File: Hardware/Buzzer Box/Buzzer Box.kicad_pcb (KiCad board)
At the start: 2 copper layers, 105.5 x 60.5 mm, 77 parts, among them IC1 4691, IC10 4691, IC11 4691, IC12 4691, IC2 4691, IC3 4691, IC4 4691, IC5 4691, IC6 4691, IC7 4691, IC8 4691, IC9 4691, J1 GPIO 2 + GND, J10 Conn_01x03_Socket, J11 USB_C_Receptacle_USB2.0_16P, J12 GPIO 2 + GND, J15 IO42, J16 IO41, J19 GND, J2 Conn_01x03_Socket, J20 3V3, J21 24V, J22 5V, J3 Conn_01x03_Socket, J4 Conn_01x03_Socket, J5 Conn_01x03_Socket, J6 GPIO 2 + GND, J7 Conn_01x03_Socket, J8 Conn_01x03_Socket, J9 Conn_01x03_Socket, Q1 AO3400A, Q2 AO3400A, Q3 AO3400A, Q4 AO3400A, Q5 AO3400A, Q6 AO3400A, Q7 AO3400A, Q8 AO3400A, U1 LTV-817S, U10 ESP32-S3-WROOM-1, U2 USBLC6-2SC6, U3 LTV-817S, U4 LTV-817S, U5 LTV-817S, U6 LTV-817S, U7 LTV-817S, U8 LTV-817S, U9 LTV-817S

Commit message: Updated the PCB
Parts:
- removed J10, J4, J5, J7, J8, J9: Conn_01x03_Socket, Connector_JST:JST_XH_B3B-XH-AM_1x03_P2.50mm_Vertical
- removed J15: IO42, Connector_Wire:SolderWirePad_1x01_SMD_1x2mm
- removed J16: IO41, Connector_Wire:SolderWirePad_1x01_SMD_1x2mm
- added C3: 100n, Capacitor_SMD:C_0603_1608Metric_Pad1.08x0.95mm_HandSolder, F.Cu at (119.8, 116.6)
- added C4: 100n, Capacitor_SMD:C_0603_1608Metric_Pad1.08x0.95mm_HandSolder, F.Cu at (137.8, 116.6)
- added C6: 100n, Capacitor_SMD:C_0603_1608Metric_Pad1.08x0.95mm_HandSolder, F.Cu at (101.8, 116.6)
- added C7: 100n, Capacitor_SMD:C_0603_1608Metric_Pad1.08x0.95mm_HandSolder, F.Cu at (84.0, 116.6)
- added H1: MountingHole_Pad, MountingHole:MountingHole_3.2mm_M3_ISO14580_Pad_TopBottom, F.Cu at (71.0, 72.0)
- added H2: MountingHole_Pad, MountingHole:MountingHole_3.2mm_M3_ISO14580_Pad_TopBottom, F.Cu at (201.0, 73.0)
- added H3: MountingHole_Pad, MountingHole:MountingHole_3.2mm_M3_ISO14580_Pad_TopBottom, F.Cu at (197.0, 109.0)
- added H4: MountingHole_Pad, MountingHole:MountingHole_3.2mm_M3_ISO14580_Pad_TopBottom, F.Cu at (47.0, 119.0)
- added H5: MountingHole_Pad, MountingHole:MountingHole_3.2mm_M3_ISO14580_Pad_TopBottom, F.Cu at (148.0, 74.0)
- added J13: NC3FAAH, Connector_Audio:Jack_XLR_Neutrik_NC3FAAH_Horizontal, F.Cu at (158.0, 68.9)
- added J14: NC3FAAH, Connector_Audio:Jack_XLR_Neutrik_NC3FAAH_Horizontal, F.Cu at (184.0, 68.9)
- added J17: NC3FAAH, Connector_Audio:Jack_XLR_Neutrik_NC3FAAH_Horizontal, F.Cu at (210.0, 68.9)
- added J18: NC3FAAH, Connector_Audio:Jack_XLR_Neutrik_NC3FAAH_Horizontal, F.Cu at (216.0, 107.0)
- added J23: NC3FAAH, Connector_Audio:Jack_XLR_Neutrik_NC3FAAH_Horizontal, F.Cu at (132.0, 68.9)
- added J24: NC3FAAH, Connector_Audio:Jack_XLR_Neutrik_NC3FAAH_Horizontal, F.Cu at (106.0, 68.9)
- added J25: NC3FAAH, Connector_Audio:Jack_XLR_Neutrik_NC3FAAH_Horizontal, F.Cu at (80.0, 68.9)
- added J26: NC3FAAH, Connector_Audio:Jack_XLR_Neutrik_NC3FAAH_Horizontal, F.Cu at (54.0, 68.9)
- C1: footprint Capacitor_SMD:C_0603_1608Metric_Pad1.08x0.95mm_HandSolder -> Capacitor_SMD:C_0603_1608Metric
- J19, J20, J22: moved to F.Cu
- J2: value Conn_01x03_Socket -> UART; footprint Connector_JST:JST_XH_B3B-XH-AM_1x03_P2.50mm_Vertical -> Connector_JST:JST_XH_B4B-XH-A_1x04_P2.50mm_Vertical
- J21: value 24V -> 24v; moved to F.Cu
- J3: value Conn_01x03_Socket -> JTAG; footprint Connector_JST:JST_XH_B3B-XH-AM_1x03_P2.50mm_Vertical -> Connector_JST:JST_XH_B4B-XH-A_1x04_P2.50mm_Vertical
- R10, R3, R4, R5, R6, R7, R8, R9: footprint Resistor_SMD:R_0805_2012Metric -> Resistor_SMD:R_0603_1608Metric
- moved R16 89.4 mm to (98.2, 107.0), turned to 0 degrees
- moved R20 86.5 mm to (77.0, 102.1), turned to 180 degrees
- moved R17 86.2 mm to (61.8, 102.1)
- moved R18 85.8 mm to (56.8, 102.1)
- moved U11 84.7 mm to (50.6, 97.0)
- moved U12 83.5 mm to (70.8, 97.0)
- moved R19 81.7 mm to (82.0, 102.1)
- moved R2 74.3 mm to (98.2, 105.0)
- moved J2 66.7 mm to (117.5, 103.5), turned to 90 degrees
- moved C1 65.3 mm to (107.5, 105.0), turned to 180 degrees
- moved R11 65.1 mm to (107.5, 107.0), turned to 0 degrees
- moved Q8 62.6 mm to (48.4, 79.2)
- moved S1 59.4 mm to (110.0, 101.2), turned to 180 degrees
- moved U9 58.3 mm to (57.4, 80.3), turned to 180 degrees
- moved IC11 55.6 mm to (143.5, 122.0)
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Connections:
- J2 pad 1: Net-(J2-Pin_1) -> GND
- J2 pad 2: +24V -> Net-(J2-Pin_2)
- J3 pad 2: +24V -> Net-(J3-Pin_2)
- J3 pad 3: Net-(J3-Pin_3) -> Net-(J12-Pin_2)
- Q1 pad 3: Net-(J3-Pin_1) -> Net-(Q1-D)
- Q2 pad 3: Net-(J2-Pin_1) -> Net-(Q2-D)
- R3 pad 1: Net-(J3-Pin_3) -> Net-(J13-Pad2)
- R4 pad 1: Net-(J2-Pin_3) -> Net-(J14-Pad2)
- U10 pad 34: Net-(J16-Pin_1) -> Net-(J3-Pin_2)
- U10 pad 35: Net-(J15-Pin_1) -> Net-(J3-Pin_1)
- U10 pad 36: unconnected-(U10-RXD0-Pad36) -> Net-(J2-Pin_3)
- U10 pad 37: unconnected-(U10-TXD0-Pad37) -> Net-(J2-Pin_2)
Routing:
- net +3.3V: track 274.1 -> 406.5 mm, vias 24 -> 10
- net +24V: track 220.3 -> 342.2 mm
- net Net-(U10-IO0): track 22.9 -> 88.0 mm, vias 0 -> 2
- net Net-(J2-Pin_2): track 0.00 -> 49.6 mm
- net Net-(IC1-DIN): track 69.9 -> 118.0 mm
- net /taster IO3/Taster: track 10.2 -> 56.1 mm
- net Net-(J2-Pin_3): track 6.04 -> 50.2 mm
- net Net-(J6-Pin_2): track 55.6 -> 12.1 mm
- net /taster IO7/Taster: track 87.1 -> 127.2 mm
- net /taster IO3/LED: track 21.0 -> 60.7 mm
- net Net-(J3-Pin_2): track 0.00 -> 37.5 mm
- net Net-(Q2-D): track 0.00 -> 37.1 mm
- net Net-(J14-Pad2): track 0.00 -> 36.7 mm
- net Net-(J13-Pad2): track 0.00 -> 36.7 mm
- net Net-(S1-COM_1): track 54.2 -> 90.2 mm
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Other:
- board size 105.5 x 60.5 mm -> 185 x 65 mm
- board text removed: "1(48 47) 2(14 13) 3(12 11) 4(10 9) 5(18 17) 6(16 15) 7(7 6) 8(5 4)"
- board text removed: "IO 40 IO 39 IO 38"
- board text removed: "JLCJLCJLCJLC"
- board text removed: "Reset IO0"

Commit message: made chages to the PCB
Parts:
- J1: value GPIO 2 + GND -> GPIO 39; footprint Connector_JST:JST_XH_B2B-XH-AM_1x02_P2.50mm_Vertical -> Connector_JST:JST_XH_B2B-XH-A_1x02_P2.50mm_Vertical
- J12: value GPIO 2 + GND -> GPIO 40; footprint Connector_JST:JST_XH_B2B-XH-AM_1x02_P2.50mm_Vertical -> Connector_JST:JST_XH_B2B-XH-A_1x02_P2.50mm_Vertical
- J6: value GPIO 2 + GND -> GPIO 38; footprint Connector_JST:JST_XH_B2B-XH-AM_1x02_P2.50mm_Vertical -> Connector_JST:JST_XH_B2B-XH-A_1x02_P2.50mm_Vertical
- moved C2 2.24 mm to (187.0, 111.1), turned to 180 degrees
- moved H5 2.24 mm to (149.0, 72.0)
- moved C8 1.51 mm to (187.0, 109.0), turned to 180 degrees
- moved H2 1.00 mm to (201.0, 72.0)
- moved Q4 0.65 mm to (221.6, 96.7)
- moved U5 0.65 mm to (212.6, 95.6)
- moved R6 0.57 mm to (204.6, 96.9), turned to 0 degrees
- moved Q3 0.30 mm to (204.4, 79.2)
- moved R10 0.30 mm to (65.4, 79.0), turned to 180 degrees
- moved R3 0.30 mm to (169.4, 79.0), turned to 180 degrees
- moved R4 0.30 mm to (195.4, 79.0), turned to 180 degrees
- moved R7 0.30 mm to (143.4, 79.0), turned to 180 degrees
- moved R8 0.30 mm to (117.4, 79.0), turned to 180 degrees
- moved R9 0.30 mm to (91.4, 79.0), turned to 180 degrees
- moved U4 0.30 mm to (213.4, 80.3)
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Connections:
- J1 pad 1: GND -> +3.3V
- J12 pad 1: GND -> +3.3V
- J6 pad 1: GND -> +3.3V
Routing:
- net +3.3V: track 406.5 -> 479.3 mm
- net +24V: track 342.2 -> 367.4 mm
- net Net-(Q4-D): track 37.1 -> 12.4 mm
- net Net-(Q2-D): track 37.1 -> 12.4 mm
- net Net-(J18-Pad2): track 36.7 -> 13.1 mm
- net Net-(J14-Pad2): track 36.7 -> 13.1 mm
- net Net-(J13-Pad2): track 36.7 -> 13.1 mm
- net Net-(Q1-D): track 24.7 -> 12.4 mm
- net Net-(J23-Pad2): track 24.4 -> 13.1 mm
- net Net-(J24-Pad2): track 24.4 -> 13.1 mm
- net Net-(R6-Pad2): track 13.2 -> 4.29 mm
- net Net-(R3-Pad2): track 13.2 -> 4.29 mm
- net Net-(J25-Pad2): track 19.2 -> 13.1 mm
- net Net-(R7-Pad2): track 8.77 -> 4.29 mm
- net Net-(R8-Pad2): track 8.77 -> 4.29 mm
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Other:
- outline, holes or cut-outs redrawn
- board text added: "JLCJLCJLCJLC"

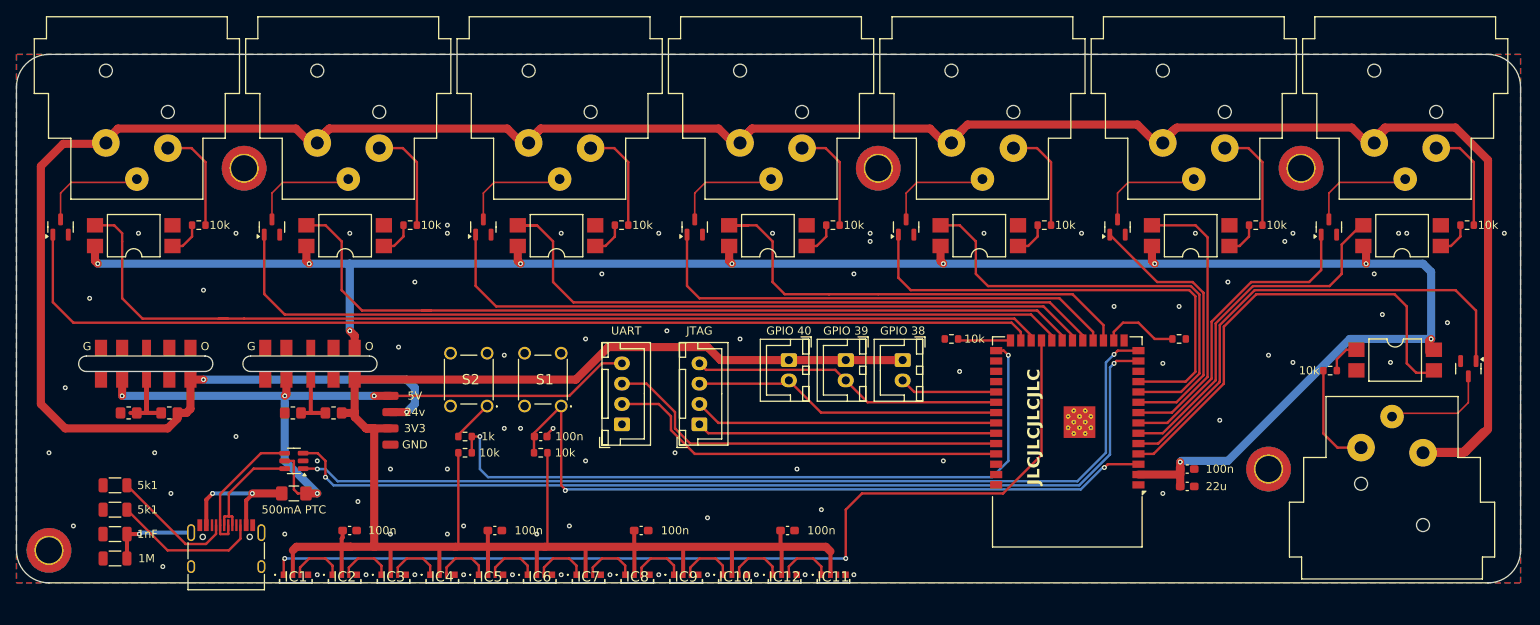
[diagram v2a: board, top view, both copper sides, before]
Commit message: chaged the usb position on pcb
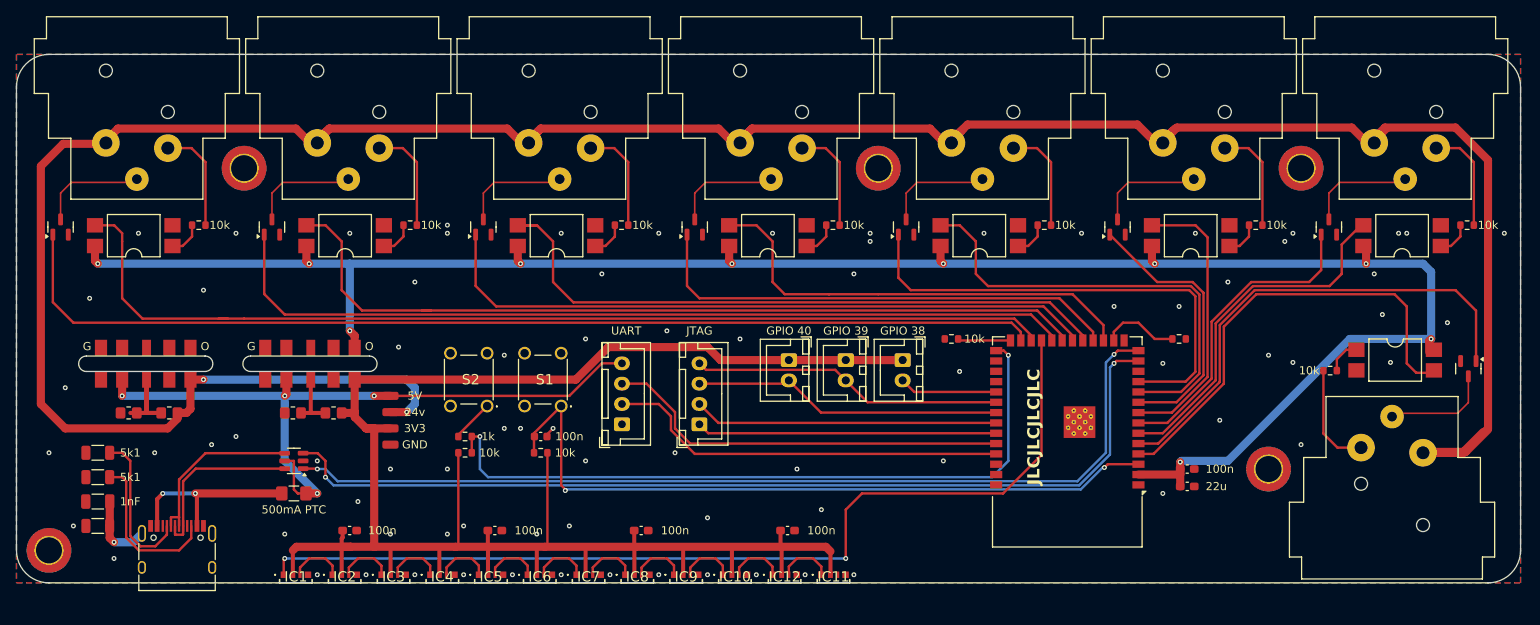
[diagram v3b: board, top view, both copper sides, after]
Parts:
- moved J11 6.05 mm to (62.8, 120.0)
- moved C5 4.53 mm to (53.0, 113.0)
- moved R1 4.53 mm to (53.0, 116.0)
- moved R12 4.53 mm to (53.0, 110.0)
- moved R13 4.53 mm to (53.0, 107.0)
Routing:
- net Net-(J11-D+-PadA6): track 14.0 -> 21.7 mm
- net Net-(F1-Pad2): track 17.0 -> 23.0 mm
- net Net-(J11-D--PadA7): track 17.0 -> 22.1 mm
- net Net-(J11-CC1): track 15.5 -> 18.9 mm
- net /taster IO4/Taster: track 58.4 -> 56.1 mm
- net Net-(J11-SHIELD): track 11.0 -> 9.11 mm
- net Net-(J11-CC2): track 18.3 -> 20.0 mm

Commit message: added debouncing caps
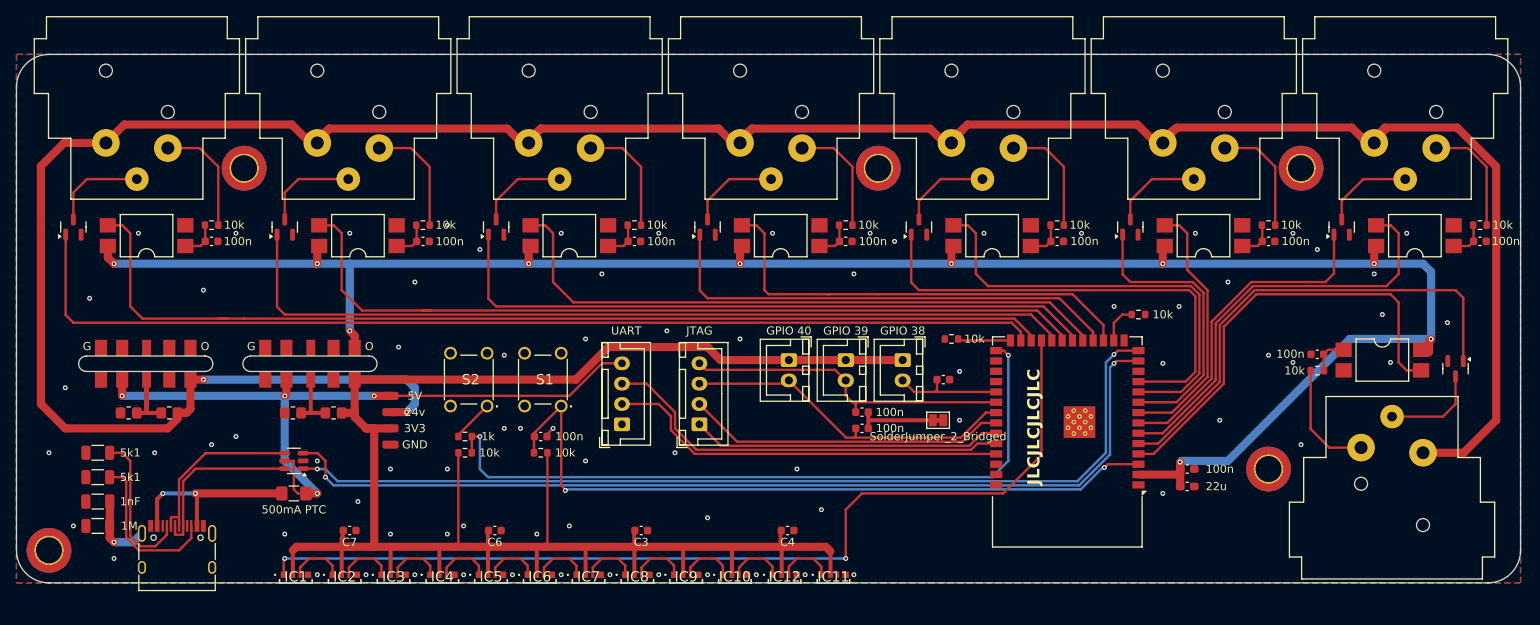
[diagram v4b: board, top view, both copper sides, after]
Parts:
- added C10: 100n, Capacitor_SMD:C_0603_1608Metric, F.Cu at (147.0, 102.0)
- added C11: 100n, Capacitor_SMD:C_0603_1608Metric, F.Cu at (157.0, 98.0)
- added C12: 100n, Capacitor_SMD:C_0603_1608Metric, F.Cu at (171.0, 81.0)
- added C13: 100n, Capacitor_SMD:C_0603_1608Metric, F.Cu at (197.0, 81.0)
- added C14: 100n, Capacitor_SMD:C_0603_1608Metric, F.Cu at (223.0, 81.0)
- added C15: 100n, Capacitor_SMD:C_0603_1608Metric, F.Cu at (203.0, 94.9)
- added C16: 100n, Capacitor_SMD:C_0603_1608Metric, F.Cu at (145.0, 81.0)
- added C17: 100n, Capacitor_SMD:C_0603_1608Metric, F.Cu at (119.0, 81.0)
- added C18: 100n, Capacitor_SMD:C_0603_1608Metric, F.Cu at (93.0, 81.0)
- added C19: 100n, Capacitor_SMD:C_0603_1608Metric, F.Cu at (67.0, 81.0)
- added C9: 100n, Capacitor_SMD:C_0603_1608Metric, F.Cu at (147.0, 104.0)
- added JP1: SolderJumper_2_Bridged, Jumper:SolderJumper-2_P1.3mm_Bridged_Pad1.0x1.5mm, F.Cu at (156.3, 103.0)
- C3, C4, C6, C7: footprint Capacitor_SMD:C_0603_1608Metric_Pad1.08x0.95mm_HandSolder -> Capacitor_SMD:C_0603_1608Metric
- moved R15 5.83 mm to (181.0, 90.0)
- moved Q5 1.58 mm to (128.0, 79.2)
- moved Q6 1.58 mm to (102.0, 79.2)
- moved Q7 1.58 mm to (76.0, 79.2)
- moved Q8 1.58 mm to (50.0, 79.2)
- moved R10 1.58 mm to (67.0, 79.0)
- moved R8 1.58 mm to (119.0, 79.0)
- moved R9 1.58 mm to (93.0, 79.0)
- moved U7 1.58 mm to (111.0, 80.3)
- moved U8 1.58 mm to (85.0, 80.3)
- moved U9 1.58 mm to (59.0, 80.3)
- moved Q1 1.57 mm to (154.0, 79.2)
- moved Q2 1.57 mm to (180.0, 79.2)
- moved Q3 1.57 mm to (206.0, 79.2)
- moved Q4 1.57 mm to (220.0, 96.7)
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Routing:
- net +24V: track 367.4 -> 351.6 mm
- net Net-(JP1-B): track 0.00 -> 9.96 mm
- net /taster IO2/Taster: track 44.9 -> 52.4 mm
- net Net-(U10-IO46): track 9.56 -> 4.79 mm
- net Net-(J12-Pin_2): track 38.3 -> 42.1 mm
- net /taster IO5/Taster: track 81.0 -> 77.7 mm
- net /taster IO1/Taster: track 34.9 -> 32.2 mm
- net Net-(J1-Pin_2): track 38.5 -> 40.9 mm
- net +3.3V: track 479.3 -> 477.2 mm
- net Net-(U11-FB): track 15.2 -> 13.2 mm
- net Net-(J3-Pin_2): track 37.5 -> 39.4 mm
- net /taster IO2/LED: track 38.7 -> 40.5 mm
- net Net-(J6-Pin_2): track 12.1 -> 13.7 mm
- net /taster IO1/LED: track 34.0 -> 35.3 mm
- net Net-(J3-Pin_1): track 37.0 -> 38.2 mm
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
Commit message: fixed lable
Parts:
- JP1: value SolderJumper_2_Bridged -> EN-JTAG
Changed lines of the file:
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@@
 		(tags "SOT TO_SOT_SMD")
 		(property "Reference" "Q4"
-			(at 0 -2.4 -270)
+			(at 0 -2.4 90)
 			(layer "F.SilkS")
 			(hide yes)
@@
 		)
 		(property "Value" "AO3400A"
-			(at 0 2.4 -270)
+			(at 0 2.4 90)
 			(layer "F.Fab")
 			(hide yes)
@@
 		)
 		(fp_text user "${REFERENCE}"
-			(at 0 0 -270)
+			(at 0 0 90)
 			(layer "F.Fab")
 			(effects
@@
 		)
 		(property "Value" "10k"
-			(at -2.79333 0.016962 -180)
+			(at -2.79333 0.016962 180)
 			(layer "F.SilkS")
 			(effects
@@
 		(tags "neutrik xlr aa")
 		(property "Reference" "J18"
-			(at 4.299999 -10 -270)
+			(at 4.299999 -10 90)
 			(layer "F.SilkS")
 			(hide yes)
@@
 		)
 		(property "Value" "NC3FAAH"
-			(at 4.3 17.5 -270)
+			(at 4.3 17.5 90)
 			(layer "F.Fab")
 			(hide yes)
@@
 			)
 		)
-		(property "Value" "SolderJumper_2_Bridged"
+		(property "Value" "EN-JTAG"
 			(at 0 -2 180)
 			(layer "F.SilkS")

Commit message: final version
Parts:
- removed J12: GPIO 40, Connector_JST:JST_XH_B2B-XH-A_1x02_P2.50mm_Vertical
- removed J3: JTAG, Connector_JST:JST_XH_B4B-XH-A_1x04_P2.50mm_Vertical
- removed JP1: EN-JTAG, Jumper:SolderJumper-2_P1.3mm_Bridged_Pad1.0x1.5mm
- added J4: GPIO 39, Connector_JST:JST_XH_B2B-XH-A_1x02_P2.50mm_Vertical, F.Cu at (138.0, 95.5)
- added J5: GPIO 39, Connector_JST:JST_XH_B2B-XH-A_1x02_P2.50mm_Vertical, F.Cu at (145.0, 95.5)
- J2: value UART -> JTAG; footprint Connector_JST:JST_XH_B4B-XH-A_1x04_P2.50mm_Vertical -> kiCadLibs:490107670612
- J6: value GPIO 38 -> UART; footprint Connector_JST:JST_XH_B2B-XH-A_1x02_P2.50mm_Vertical -> kiCadLibs:490107670612
- moved J6 35.8 mm to (116.7, 101.8)
- moved C11 13.6 mm to (144.0, 102.0), turned to 0 degrees
- moved C9 10.2 mm to (137.0, 102.0), turned to 0 degrees
- moved J2 9.41 mm to (126.7, 101.8), turned to -90 degrees
- moved J1 7.00 mm to (152.0, 95.5)
- moved C10 4.00 mm to (151.0, 102.0), turned to 0 degrees
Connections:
- C1 pad 2: Net-(S1-COM_1) -> RST
- C10 pad 1: Net-(JP1-B) -> GND
- C10 pad 2: Net-(J1-Pin_2) -> /IOin/out
- C11 pad 2: Net-(J6-Pin_2) -> /IOin2/out
- C9 pad 1: Net-(JP1-B) -> GND
- C9 pad 2: Net-(J12-Pin_2) -> /IOin1/out
- J1 pad 2: Net-(J1-Pin_2) -> /IOin/out
- J2 pad 1: GND -> +3.3V
- J2 pad 2: Net-(J2-Pin_2) -> MTMS
- J2 pad 3: Net-(J2-Pin_3) -> MTDI
- J2 pad 4: +5V -> MTCK
- J6 pad 2: Net-(J6-Pin_2) -> RST
- R11 pad 1: Net-(S1-COM_1) -> RST
- R16 pad 2: Net-(U10-IO0) -> OI0
- R2 pad 1: Net-(U10-IO0) -> OI0
- S1 pad 1: Net-(S1-COM_1) -> RST
- U10 pad 27: Net-(U10-IO0) -> OI0
- U10 pad 3: Net-(S1-COM_1) -> RST
- U10 pad 31: Net-(J6-Pin_2) -> /IOin/out
- U10 pad 32: Net-(J1-Pin_2) -> MTCK
- U10 pad 33: Net-(J12-Pin_2) -> MTDO
- U10 pad 34: Net-(J3-Pin_2) -> MTDI
- U10 pad 35: Net-(J3-Pin_1) -> MTMS
- U10 pad 36: Net-(J2-Pin_3) -> RX0
- U10 pad 37: Net-(J2-Pin_2) -> TX0
- U10 pad 38: unconnected-(U10-IO2-Pad38) -> /IOin2/out
- U10 pad 39: unconnected-(U10-IO1-Pad39) -> /IOin1/out
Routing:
- net OI0: track 0.00 -> 108.1 mm, vias 0 -> 2
- net RST: track 0.00 -> 96.7 mm, vias 0 -> 2
- net Net-(S1-COM_1): track 90.2 -> 0.00 mm, vias 2 -> 0
- net Net-(U10-IO0): track 88.0 -> 0.00 mm, vias 2 -> 0
- net RX0: track 0.00 -> 54.2 mm
- net MTCK: track 0.00 -> 53.6 mm
- net Net-(J2-Pin_3): track 50.9 -> 0.00 mm
- net TX0: track 0.00 -> 50.3 mm
- net Net-(J2-Pin_2): track 49.6 -> 0.00 mm
- net Net-(J12-Pin_2): track 42.1 -> 0.00 mm
- net Net-(J1-Pin_2): track 40.9 -> 0.00 mm
- net MTDO: track 0.00 -> 40.6 mm
- net MTMS: track 0.00 -> 39.7 mm
- net Net-(J3-Pin_2): track 39.4 -> 0.00 mm
- net Net-(J3-Pin_1): track 38.2 -> 0.00 mm
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
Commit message: some changes
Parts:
- C2, C8: footprint Capacitor_SMD:C_0603_1608Metric_Pad1.08x0.95mm_HandSolder -> Capacitor_SMD:C_0603_1608Metric
- IC1, IC10, IC11, IC12, IC2, IC3, IC4, IC5, IC6, IC7, IC8, IC9: footprint KiCad:4691 -> Felix_LED:4691
- J13, J14, J17, J18, J23, J24, J25, J26: footprint Connector_Audio:Jack_XLR_Neutrik_NC3FAAH_Horizontal -> Felix_XLR:Jack_XLR_Neutrik_NC3FAAH_Horizontal
- J2, J6: footprint kiCadLibs:490107670612 -> Felix_ProgHeader:490107670612

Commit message: fixed design
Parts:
- moved J18 3.57 mm to (216.4, 110.6)
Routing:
- net +24V: track 351.6 -> 356.0 mm
- net Net-(J18-Pad2): track 14.3 -> 18.1 mm
- net Net-(Q4-D): track 11.9 -> 14.7 mm
